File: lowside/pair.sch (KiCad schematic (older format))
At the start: 13 parts, among them U1 VNLD5090

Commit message: add 7th pair
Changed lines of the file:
@@
 $Descr A4 11693 8268
 encoding utf-8
-Sheet 2 7
+Sheet 8 8
 Title ""
 Date ""
@@
 AR Path="/5E2D1A09/5E28FEFB" Ref="U5"  Part="1"
 AR Path="/5E2D1A0F/5E28FEFB" Ref="U6"  Part="1"
-F 0 "U1" H 3100 2547 60  0000 C CNN
+AR Path="/5E2B6330/5E28FEFB" Ref="U7"  Part="1"
+F 0 "U7" H 3100 2547 60  0000 C CNN
 F 1 "VNLD5090" H 3100 2441 60  0000 C CNN
 F 2 "Package_SO:SO-8_3.9x4.9mm_P1.27mm" H 3200 1650 60  0001 C CNN
@@
 AR Path="/5E2D1A09/5E290D55" Ref="#PWR0153"  Part="1"
 AR Path="/5E2D1A0F/5E290D55" Ref="#PWR0163"  Part="1"
-F 0 "#PWR0113" H 3300 2250 50  0001 C CNN
+AR Path="/5E2B6330/5E290D55" Ref="#PWR0177"  Part="1"
+F 0 "#PWR0177" H 3300 2250 50  0001 C CNN
 F 1 "GND" H 3305 2327 50  0000 C CNN
 F 2 "" H 3300 2500 50  0001 C CNN
@@
 AR Path="/5E2D1A09/5E291066" Ref="#PWR0154"  Part="1"
 AR Path="/5E2D1A0F/5E291066" Ref="#PWR0164"  Part="1"
-F 0 "#PWR0114" H 3400 2250 50  0001 C CNN
+AR Path="/5E2B6330/5E291066" Ref="#PWR0178"  Part="1"
+F 0 "#PWR0178" H 3400 2250 50  0001 C CNN
 F 1 "GND" H 3405 2327 50  0000 C CNN
 F 2 "" H 3400 2500 50  0001 C CNN
@@
 AR Path="/5E2D1A09/5E291CC1" Ref="R25"  Part="1"
 AR Path="/5E2D1A0F/5E291CC1" Ref="R31"  Part="1"
-F 0 "R1" V 2100 1500 50  0000 C CNN
+AR Path="/5E2B6330/5E291CC1" Ref="R39"  Part="1"
+F 0 "R39" V 2100 1500 50  0000 C CNN
 F 1 "1k" V 2200 1500 50  0000 C CNN
 F 2 "Resistor_SMD:R_0603_1608Metric" V 2130 1500 50  0001 C CNN
@@
 AR Path="/5E2D1A09/5E292256" Ref="R26"  Part="1"
 AR Path="/5E2D1A0F/5E292256" Ref="R32"  Part="1"
-F 0 "R2" V 2300 2050 50  0000 C CNN
+AR Path="/5E2B6330/5E292256" Ref="R40"  Part="1"
+F 0 "R40" V 2300 2050 50  0000 C CNN
 F 1 "1k" V 2200 2050 50  0000 C CNN
 F 2 "Resistor_SMD:R_0603_1608Metric" V 2130 2050 50  0001 C CNN
@@
 AR Path="/5E2D1A09/5E2928C2" Ref="C9"  Part="1"
 AR Path="/5E2D1A0F/5E2928C2" Ref="C11"  Part="1"
-F 0 "C1" H 3635 1204 50  0000 R CNN
+AR Path="/5E2B6330/5E2928C2" Ref="C13"  Part="1"
+F 0 "C13" H 3635 1204 50  0000 R CNN
 F 1 "6.8n" H 3635 1295 50  0000 R CNN
 F 2 "Capacitor_SMD:C_0603_1608Metric" H 3788 1100 50  0001 C CNN
@@
 AR Path="/5E2D1A09/5E293060" Ref="C10"  Part="1"
 AR Path="/5E2D1A0F/5E293060" Ref="C12"  Part="1"
-F 0 "C2" H 3865 2346 50  0000 L CNN
+AR Path="/5E2B6330/5E293060" Ref="C14"  Part="1"
+F 0 "C14" H 3865 2346 50  0000 L CNN
 F 1 "6.8n" H 3865 2255 50  0000 L CNN
 F 2 "Capacitor_SMD:C_0603_1608Metric" H 3788 2150 50  0001 C CNN
@@
 AR Path="/5E2D1A09/5E293508" Ref="#PWR0155"  Part="1"
 AR Path="/5E2D1A0F/5E293508" Ref="#PWR0165"  Part="1"
-F 0 "#PWR0115" H 3750 850 50  0001 C CNN
+AR Path="/5E2B6330/5E293508" Ref="#PWR0179"  Part="1"
+F 0 "#PWR0179" H 3750 850 50  0001 C CNN
 F 1 "GND" H 3755 927 50  0000 C CNN
 F 2 "" H 3750 1100 50  0001 C CNN
@@
 AR Path="/5E2D1A09/5E294C43" Ref="#PWR0156"  Part="1"
 AR Path="/5E2D1A0F/5E294C43" Ref="#PWR0166"  Part="1"
-F 0 "#PWR0116" H 3750 2200 50  0001 C CNN
+AR Path="/5E2B6330/5E294C43" Ref="#PWR0180"  Part="1"
+F 0 "#PWR0180" H 3750 2200 50  0001 C CNN
 F 1 "GND" H 3755 2277 50  0000 C CNN
 F 2 "" H 3750 2450 50  0001 C CNN
@@
 AR Path="/5E2D1A09/5E295706" Ref="#PWR0157"  Part="1"
 AR Path="/5E2D1A0F/5E295706" Ref="#PWR0167"  Part="1"
-F 0 "#PWR0117" H 2450 2350 50  0001 C CNN
+AR Path="/5E2B6330/5E295706" Ref="#PWR0181"  Part="1"
+F 0 "#PWR0181" H 2450 2350 50  0001 C CNN
 F 1 "GND" H 2455 2427 50  0000 C CNN
 F 2 "" H 2450 2600 50  0001 C CNN
@@
 AR Path="/5E2D1A09/5E295C01" Ref="R28"  Part="1"
 AR Path="/5E2D1A0F/5E295C01" Ref="R34"  Part="1"
-F 0 "R4" V 2350 2400 50  0000 L CNN
+AR Path="/5E2B6330/5E295C01" Ref="R42"  Part="1"
+F 0 "R42" V 2350 2400 50  0000 L CNN
 F 1 "10k" V 2450 2350 50  0000 L CNN
 F 2 "Resistor_SMD:R_0603_1608Metric" V 2380 2450 50  0001 C CNN
@@
 AR Path="/5E2D1A09/5E295EF2" Ref="R27"  Part="1"
 AR Path="/5E2D1A0F/5E295EF2" Ref="R33"  Part="1"
-F 0 "R3" V 2550 1200 50  0000 L CNN
+AR Path="/5E2B6330/5E295EF2" Ref="R41"  Part="1"
+F 0 "R41" V 2550 1200 50  0000 L CNN
 F 1 "10k" V 2450 1200 50  0000 L CNN
 F 2 "Resistor_SMD:R_0603_1608Metric" V 2380 1250 50  0001 C CNN
@@
 AR Path="/5E2D1A09/5E297A73" Ref="#PWR0158"  Part="1"
 AR Path="/5E2D1A0F/5E297A73" Ref="#PWR0168"  Part="1"
-F 0 "#PWR0118" H 2450 850 50  0001 C CNN
+AR Path="/5E2B6330/5E297A73" Ref="#PWR0182"  Part="1"
+F 0 "#PWR0182" H 2450 850 50  0001 C CNN
 F 1 "GND" H 2455 927 50  0000 C CNN
 F 2 "" H 2450 1100 50  0001 C CNN
@@
 AR Path="/5E2D1A09/5E2A21C5" Ref="D17"  Part="1"
 AR Path="/5E2D1A0F/5E2A21C5" Ref="D21"  Part="1"
-F 0 "D1" V 4204 1329 50  0000 L CNN
+AR Path="/5E2B6330/5E2A21C5" Ref="D27"  Part="1"
+F 0 "D27" V 4204 1329 50  0000 L CNN
 F 1 "D_Schottky" V 4295 1329 50  0000 L CNN
 F 2 "Diode_SMD:D_SMF" H 4250 1250 50  0001 C CNN
@@
 AR Path="/5E2D1A09/5E2A29A5" Ref="#PWR0159"  Part="1"
 AR Path="/5E2D1A0F/5E2A29A5" Ref="#PWR0169"  Part="1"
-F 0 "#PWR0137" H 4250 950 50  0001 C CNN
+AR Path="/5E2B6330/5E2A29A5" Ref="#PWR0183"  Part="1"
+F 0 "#PWR0183" H 4250 950 50  0001 C CNN
 F 1 "+12V" H 4265 1273 50  0000 C CNN
 F 2 "" H 4250 1100 50  0001 C CNN
@@
 AR Path="/5E2D1A09/5E2A30AB" Ref="D18"  Part="1"
 AR Path="/5E2D1A0F/5E2A30AB" Ref="D22"  Part="1"
-F 0 "D2" V 4296 2221 50  0000 R CNN
+AR Path="/5E2B6330/5E2A30AB" Ref="D28"  Part="1"
+F 0 "D28" V 4296 2221 50  0000 R CNN
 F 1 "D_Schottky" V 4205 2221 50  0000 R CNN
 F 2 "Diode_SMD:D_SMF" H 4250 2300 50  0001 C CNN
@@
 AR Path="/5E2D1A09/5E2A3E5A" Ref="#PWR0160"  Part="1"
 AR Path="/5E2D1A0F/5E2A3E5A" Ref="#PWR0170"  Part="1"
-F 0 "#PWR0138" H 4250 2300 50  0001 C CNN
+AR Path="/5E2B6330/5E2A3E5A" Ref="#PWR0184"  Part="1"
+F 0 "#PWR0184" H 4250 2300 50  0001 C CNN
 F 1 "+12V" H 4265 2623 50  0000 C CNN
 F 2 "" H 4250 2450 50  0001 C CNN
@@
 AR Path="/5E2D1A09/5E2BF0E5" Ref="D20"  Part="1"
 AR Path="/5E2D1A0F/5E2BF0E5" Ref="D24"  Part="1"
-F 0 "D10" V 4897 2378 50  0000 L CNN
+AR Path="/5E2B6330/5E2BF0E5" Ref="D30"  Part="1"
+F 0 "D30" V 4897 2378 50  0000 L CNN
 F 1 "LED" V 4988 2378 50  0000 L CNN
 F 2 "LED_SMD:LED_0603_1608Metric" H 4950 2300 50  0001 C CNN
@@
 AR Path="/5E2D1A09/5E2C027A" Ref="#PWR0161"  Part="1"
 AR Path="/5E2D1A0F/5E2C027A" Ref="#PWR0171"  Part="1"
-F 0 "#PWR0145" H 4950 2600 50  0001 C CNN
+AR Path="/5E2B6330/5E2C027A" Ref="#PWR0185"  Part="1"
+F 0 "#PWR0185" H 4950 2600 50  0001 C CNN
 F 1 "+12V" H 4965 2923 50  0000 C CNN
 F 2 "" H 4950 2750 50  0001 C CNN
@@
 AR Path="/5E2D1A09/5E2C0BF3" Ref="R30"  Part="1"
 AR Path="/5E2D1A0F/5E2C0BF3" Ref="R36"  Part="1"
-F 0 "R18" H 5020 2646 50  0000 L CNN
+AR Path="/5E2B6330/5E2C0BF3" Ref="R44"  Part="1"
+F 0 "R44" H 5020 2646 50  0000 L CNN
 F 1 "1k" H 5020 2555 50  0000 L CNN
 F 2 "Resistor_SMD:R_0603_1608Metric" V 4880 2600 50  0001 C CNN
@@
 AR Path="/5E2D1A09/5E2C1564" Ref="D19"  Part="1"
 AR Path="/5E2D1A0F/5E2C1564" Ref="D23"  Part="1"
-F 0 "D9" V 4989 1133 50  0000 R CNN
+AR Path="/5E2B6330/5E2C1564" Ref="D29"  Part="1"
+F 0 "D29" V 4989 1133 50  0000 R CNN
 F 1 "LED" V 4898 1133 50  0000 R CNN
 F 2 "LED_SMD:LED_0603_1608Metric" H 4950 1250 50  0001 C CNN
@@
 AR Path="/5E2D1A09/5E2C1FBA" Ref="R29"  Part="1"
 AR Path="/5E2D1A0F/5E2C1FBA" Ref="R35"  Part="1"
-F 0 "R17" H 4880 904 50  0000 R CNN
+AR Path="/5E2B6330/5E2C1FBA" Ref="R43"  Part="1"
+F 0 "R43" H 4880 904 50  0000 R CNN
 F 1 "1k" H 4880 995 50  0000 R CNN
 F 2 "Resistor_SMD:R_0603_1608Metric" V 4880 950 50  0001 C CNN
@@
 AR Path="/5E2D1A09/5E2C2529" Ref="#PWR0162"  Part="1"
 AR Path="/5E2D1A0F/5E2C2529" Ref="#PWR0172"  Part="1"
-F 0 "#PWR0146" H 4950 650 50  0001 C CNN
+AR Path="/5E2B6330/5E2C2529" Ref="#PWR0186"  Part="1"
+F 0 "#PWR0186" H 4950 650 50  0001 C CNN
 F 1 "+12V" H 4965 973 50  0000 C CNN
 F 2 "" H 4950 800 50  0001 C CNN

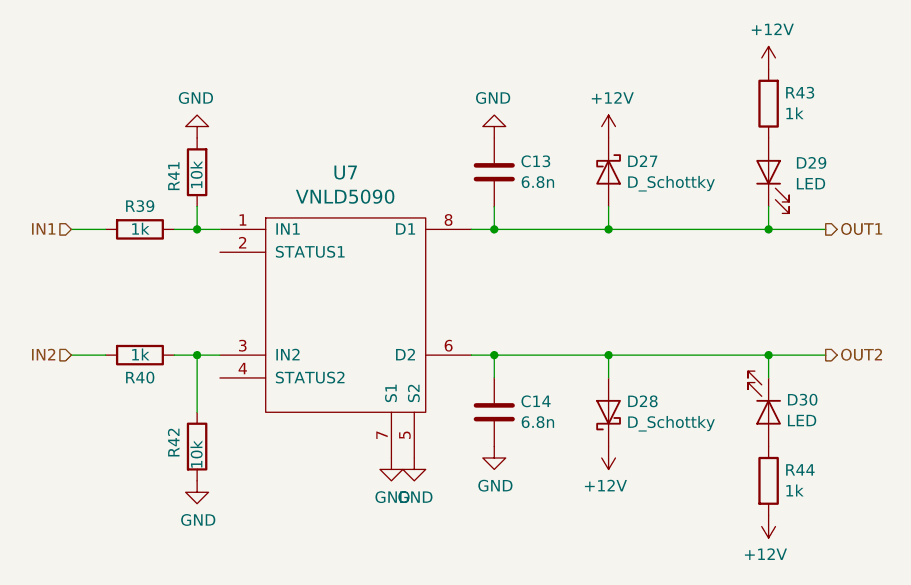
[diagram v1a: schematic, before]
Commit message: Updated properties in schematic closer to allowing BOM export.
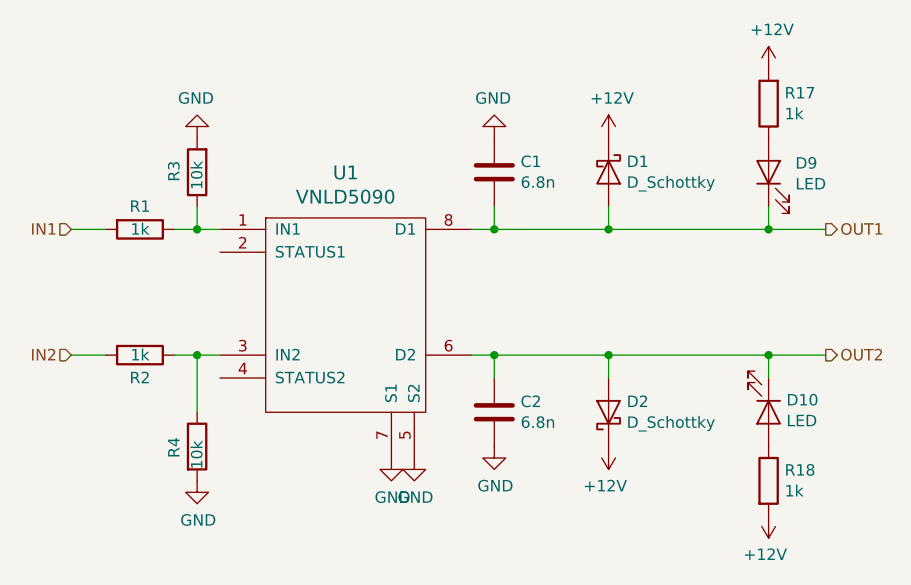
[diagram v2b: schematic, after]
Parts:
- C1, C2: MFG,MFG# (none) -> KE MET,C0603C682K1RACTU; Vend1,Vend1# (none) -> DIGI,399-3187-1-ND
- D1, D2: MFG,MFG# (none) -> LITTELFUSE,TPSMF4L36A; Vend1,Vend1# (none) -> DIGI,F7526CT-ND
- D15, D16: MFG,MFG# (none) -> DIALIGHT,598-8010-107F; Vend1,Vend1# (none) -> DIGI,350-2029-1-ND
- R1, R2, R23, R24: MFG,MFG# (none) -> YAGEO,RC0603JR-071KL; Vend1,Vend1# (none) -> DIGI,311-1.0KGRCT-ND
- R3, R4: MFG,MFG# (none) -> YAGEO,RC0603JR-0710KL; Vend1,Vend1# (none) -> DIGI,311-10KGRCT-ND
- U1: MFG,MFG# (none) -> ST,VNLD5090TR-E; Vend1,Vend1# (none) -> DIGI,497-14323-1-ND
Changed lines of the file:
@@
 $Descr A4 11693 8268
 encoding utf-8
-Sheet 8 8
+Sheet 2 8
 Title ""
 Date ""
@@
 AR Path="/5E2D1A0F/5E28FEFB" Ref="U6"  Part="1"
 AR Path="/5E2B6330/5E28FEFB" Ref="U7"  Part="1"
-F 0 "U7" H 3100 2547 60  0000 C CNN
+F 0 "U1" H 3100 2547 60  0000 C CNN
 F 1 "VNLD5090" H 3100 2441 60  0000 C CNN
 F 2 "Package_SO:SO-8_3.9x4.9mm_P1.27mm" H 3200 1650 60  0001 C CNN
 F 3 "" H 3200 1650 60  0001 C CNN
+F 4 "ST,VNLD5090TR-E" H 3100 1900 50  0001 C CNN "MFG,MFG#"
+F 5 "DIGI,497-14323-1-ND" H 3100 1900 50  0001 C CNN "Vend1,Vend1#"
 	1    3100 1900
 	1    0    0    -1
@@
 AR Path="/5E2D1A0F/5E290D55" Ref="#PWR0163"  Part="1"
 AR Path="/5E2B6330/5E290D55" Ref="#PWR0177"  Part="1"
-F 0 "#PWR0177" H 3300 2250 50  0001 C CNN
+F 0 "#PWR0113" H 3300 2250 50  0001 C CNN
 F 1 "GND" H 3305 2327 50  0000 C CNN
 F 2 "" H 3300 2500 50  0001 C CNN
@@
 AR Path="/5E2D1A0F/5E291066" Ref="#PWR0164"  Part="1"
 AR Path="/5E2B6330/5E291066" Ref="#PWR0178"  Part="1"
-F 0 "#PWR0178" H 3400 2250 50  0001 C CNN
+F 0 "#PWR0114" H 3400 2250 50  0001 C CNN
 F 1 "GND" H 3405 2327 50  0000 C CNN
 F 2 "" H 3400 2500 50  0001 C CNN
@@
 AR Path="/5E2D1A0F/5E291CC1" Ref="R31"  Part="1"
 AR Path="/5E2B6330/5E291CC1" Ref="R39"  Part="1"
-F 0 "R39" V 2100 1500 50  0000 C CNN
+F 0 "R1" V 2100 1500 50  0000 C CNN
 F 1 "1k" V 2200 1500 50  0000 C CNN
 F 2 "Resistor_SMD:R_0603_1608Metric" V 2130 1500 50  0001 C CNN
 F 3 "~" H 2200 1500 50  0001 C CNN
+F 4 "YAGEO,RC0603JR-071KL" H 2200 1500 50  0001 C CNN "MFG,MFG#"
+F 5 "DIGI,311-1.0KGRCT-ND" H 2200 1500 50  0001 C CNN "Vend1,Vend1#"
 	1    2200 1500
 	0    1    1    0
@@
 AR Path="/5E2D1A0F/5E292256" Ref="R32"  Part="1"
 AR Path="/5E2B6330/5E292256" Ref="R40"  Part="1"
-F 0 "R40" V 2300 2050 50  0000 C CNN
+F 0 "R2" V 2300 2050 50  0000 C CNN
 F 1 "1k" V 2200 2050 50  0000 C CNN
 F 2 "Resistor_SMD:R_0603_1608Metric" V 2130 2050 50  0001 C CNN
 F 3 "~" H 2200 2050 50  0001 C CNN
+F 4 "YAGEO,RC0603JR-071KL" H 2200 2050 50  0001 C CNN "MFG,MFG#"
+F 5 "DIGI,311-1.0KGRCT-ND" H 2200 2050 50  0001 C CNN "Vend1,Vend1#"
 	1    2200 2050
 	0    1    1    0
@@
 AR Path="/5E2D1A0F/5E2928C2" Ref="C11"  Part="1"
 AR Path="/5E2B6330/5E2928C2" Ref="C13"  Part="1"
-F 0 "C13" H 3635 1204 50  0000 R CNN
+F 0 "C1" H 3635 1204 50  0000 R CNN
 F 1 "6.8n" H 3635 1295 50  0000 R CNN
 F 2 "Capacitor_SMD:C_0603_1608Metric" H 3788 1100 50  0001 C CNN
 F 3 "~" H 3750 1250 50  0001 C CNN
+F 4 "KE MET,C0603C682K1RACTU" H 3750 1250 50  0001 C CNN "MFG,MFG#"
+F 5 "DIGI,399-3187-1-ND" H 3750 1250 50  0001 C CNN "Vend1,Vend1#"
 	1    3750 1250
 	-1   0    0    1
@@
 AR Path="/5E2D1A0F/5E293060" Ref="C12"  Part="1"
 AR Path="/5E2B6330/5E293060" Ref="C14"  Part="1"
-F 0 "C14" H 3865 2346 50  0000 L CNN
+F 0 "C2" H 3865 2346 50  0000 L CNN
 F 1 "6.8n" H 3865 2255 50  0000 L CNN
 F 2 "Capacitor_SMD:C_0603_1608Metric" H 3788 2150 50  0001 C CNN
 F 3 "~" H 3750 2300 50  0001 C CNN
+F 4 "KE MET,C0603C682K1RACTU" H 3750 2300 50  0001 C CNN "MFG,MFG#"
+F 5 "DIGI,399-3187-1-ND" H 3750 2300 50  0001 C CNN "Vend1,Vend1#"
 	1    3750 2300
 	1    0    0    -1
@@
 AR Path="/5E2D1A0F/5E293508" Ref="#PWR0165"  Part="1"
 AR Path="/5E2B6330/5E293508" Ref="#PWR0179"  Part="1"
-F 0 "#PWR0179" H 3750 850 50  0001 C CNN
+F 0 "#PWR0115" H 3750 850 50  0001 C CNN
 F 1 "GND" H 3755 927 50  0000 C CNN
 F 2 "" H 3750 1100 50  0001 C CNN
@@
 AR Path="/5E2D1A0F/5E294C43" Ref="#PWR0166"  Part="1"
 AR Path="/5E2B6330/5E294C43" Ref="#PWR0180"  Part="1"
-F 0 "#PWR0180" H 3750 2200 50  0001 C CNN
+F 0 "#PWR0116" H 3750 2200 50  0001 C CNN
 F 1 "GND" H 3755 2277 50  0000 C CNN
 F 2 "" H 3750 2450 50  0001 C CNN
@@
 AR Path="/5E2D1A0F/5E295706" Ref="#PWR0167"  Part="1"
 AR Path="/5E2B6330/5E295706" Ref="#PWR0181"  Part="1"
-F 0 "#PWR0181" H 2450 2350 50  0001 C CNN
+F 0 "#PWR0117" H 2450 2350 50  0001 C CNN
 F 1 "GND" H 2455 2427 50  0000 C CNN
 F 2 "" H 2450 2600 50  0001 C CNN
@@
 AR Path="/5E2D1A0F/5E295C01" Ref="R34"  Part="1"
 AR Path="/5E2B6330/5E295C01" Ref="R42"  Part="1"
-F 0 "R42" V 2350 2400 50  0000 L CNN
+F 0 "R4" V 2350 2400 50  0000 L CNN
 F 1 "10k" V 2450 2350 50  0000 L CNN
 F 2 "Resistor_SMD:R_0603_1608Metric" V 2380 2450 50  0001 C CNN
 F 3 "~" H 2450 2450 50  0001 C CNN
+F 4 "YAGEO,RC0603JR-0710KL" H 2450 2450 50  0001 C CNN "MFG,MFG#"
+F 5 "DIGI,311-10KGRCT-ND" H 2450 2450 50  0001 C CNN "Vend1,Vend1#"
 	1    2450 2450
 	1    0    0    -1
@@
 AR Path="/5E2D1A0F/5E295EF2" Ref="R33"  Part="1"
 AR Path="/5E2B6330/5E295EF2" Ref="R41"  Part="1"
-F 0 "R41" V 2550 1200 50  0000 L CNN
+F 0 "R3" V 2550 1200 50  0000 L CNN
 F 1 "10k" V 2450 1200 50  0000 L CNN
 F 2 "Resistor_SMD:R_0603_1608Metric" V 2380 1250 50  0001 C CNN
 F 3 "~" H 2450 1250 50  0001 C CNN
+F 4 "YAGEO,RC0603JR-0710KL" H 2450 1250 50  0001 C CNN "MFG,MFG#"
+F 5 "DIGI,311-10KGRCT-ND" H 2450 1250 50  0001 C CNN "Vend1,Vend1#"
 	1    2450 1250
 	-1   0    0    1
@@
 AR Path="/5E2D1A0F/5E297A73" Ref="#PWR0168"  Part="1"
 AR Path="/5E2B6330/5E297A73" Ref="#PWR0182"  Part="1"
-F 0 "#PWR0182" H 2450 850 50  0001 C CNN
+F 0 "#PWR0118" H 2450 850 50  0001 C CNN
 F 1 "GND" H 2455 927 50  0000 C CNN
 F 2 "" H 2450 1100 50  0001 C CNN
@@
 AR Path="/5E2D1A0F/5E2A21C5" Ref="D21"  Part="1"
 AR Path="/5E2B6330/5E2A21C5" Ref="D27"  Part="1"
-F 0 "D27" V 4204 1329 50  0000 L CNN
+F 0 "D1" V 4204 1329 50  0000 L CNN
 F 1 "D_Schottky" V 4295 1329 50  0000 L CNN
 F 2 "Diode_SMD:D_SMF" H 4250 1250 50  0001 C CNN
 F 3 "~" H 4250 1250 50  0001 C CNN
+F 4 "LITTELFUSE,TPSMF4L36A" H 4250 1250 50  0001 C CNN "MFG,MFG#"
+F 5 "DIGI,F7526CT-ND" H 4250 1250 50  0001 C CNN "Vend1,Vend1#"
 	1    4250 1250
 	0    1    1    0
@@
 AR Path="/5E2D1A0F/5E2A29A5" Ref="#PWR0169"  Part="1"
 AR Path="/5E2B6330/5E2A29A5" Ref="#PWR0183"  Part="1"
-F 0 "#PWR0183" H 4250 950 50  0001 C CNN
+F 0 "#PWR0137" H 4250 950 50  0001 C CNN
 F 1 "+12V" H 4265 1273 50  0000 C CNN
 F 2 "" H 4250 1100 50  0001 C CNN
@@
 AR Path="/5E2D1A0F/5E2A30AB" Ref="D22"  Part="1"
 AR Path="/5E2B6330/5E2A30AB" Ref="D28"  Part="1"
-F 0 "D28" V 4296 2221 50  0000 R CNN
+F 0 "D2" V 4296 2221 50  0000 R CNN
 F 1 "D_Schottky" V 4205 2221 50  0000 R CNN
 F 2 "Diode_SMD:D_SMF" H 4250 2300 50  0001 C CNN
 F 3 "~" H 4250 2300 50  0001 C CNN
+F 4 "LITTELFUSE,TPSMF4L36A" H 4250 2300 50  0001 C CNN "MFG,MFG#"
+F 5 "DIGI,F7526CT-ND" H 4250 2300 50  0001 C CNN "Vend1,Vend1#"
 	1    4250 2300
 	0    -1   -1   0
@@
 AR Path="/5E2D1A0F/5E2A3E5A" Ref="#PWR0170"  Part="1"
 AR Path="/5E2B6330/5E2A3E5A" Ref="#PWR0184"  Part="1"
-F 0 "#PWR0184" H 4250 2300 50  0001 C CNN
+F 0 "#PWR0138" H 4250 2300 50  0001 C CNN
 F 1 "+12V" H 4265 2623 50  0000 C CNN
 F 2 "" H 4250 2450 50  0001 C CNN
@@
 AR Path="/5E2D1A0F/5E2BF0E5" Ref="D24"  Part="1"
 AR Path="/5E2B6330/5E2BF0E5" Ref="D30"  Part="1"
-F 0 "D30" V 4897 2378 50  0000 L CNN
+F 0 "D10" V 4897 2378 50  0000 L CNN
 F 1 "LED" V 4988 2378 50  0000 L CNN
 F 2 "LED_SMD:LED_0603_1608Metric" H 4950 2300 50  0001 C CNN
 F 3 "~" H 4950 2300 50  0001 C CNN
+F 4 "DIALIGHT,598-8010-107F" H 4950 2300 50  0001 C CNN "MFG,MFG#"
+F 5 "DIGI,350-2029-1-ND" H 4950 2300 50  0001 C CNN "Vend1,Vend1#"
 	1    4950 2300
 	0    1    1    0
@@
 AR Path="/5E2D1A0F/5E2C027A" Ref="#PWR0171"  Part="1"
 AR Path="/5E2B6330/5E2C027A" Ref="#PWR0185"  Part="1"
-F 0 "#PWR0185" H 4950 2600 50  0001 C CNN
+F 0 "#PWR0145" H 4950 2600 50  0001 C CNN
 F 1 "+12V" H 4965 2923 50  0000 C CNN
 F 2 "" H 4950 2750 50  0001 C CNN
@@
 AR Path="/5E2D1A0F/5E2C0BF3" Ref="R36"  Part="1"
 AR Path="/5E2B6330/5E2C0BF3" Ref="R44"  Part="1"
-F 0 "R44" H 5020 2646 50  0000 L CNN
+F 0 "R18" H 5020 2646 50  0000 L CNN
 F 1 "1k" H 5020 2555 50  0000 L CNN
 F 2 "Resistor_SMD:R_0603_1608Metric" V 4880 2600 50  0001 C CNN
 F 3 "~" H 4950 2600 50  0001 C CNN
+F 4 "YAGEO,RC0603JR-071KL" H 4950 2600 50  0001 C CNN "MFG,MFG#"
+F 5 "DIGI,311-1.0KGRCT-ND" H 4950 2600 50  0001 C CNN "Vend1,Vend1#"
 	1    4950 2600
 	1    0    0    -1
@@
 AR Path="/5E2D1A0F/5E2C1564" Ref="D23"  Part="1"
 AR Path="/5E2B6330/5E2C1564" Ref="D29"  Part="1"
-F 0 "D29" V 4989 1133 50  0000 R CNN
+F 0 "D9" V 4989 1133 50  0000 R CNN
 F 1 "LED" V 4898 1133 50  0000 R CNN
 F 2 "LED_SMD:LED_0603_1608Metric" H 4950 1250 50  0001 C CNN
 F 3 "~" H 4950 1250 50  0001 C CNN
+F 4 "DIALIGHT,598-8010-107F" H 4950 1250 50  0001 C CNN "MFG,MFG#"
+F 5 "DIGI,350-2029-1-ND" H 4950 1250 50  0001 C CNN "Vend1,Vend1#"
 	1    4950 1250
 	0    -1   -1   0
@@
 AR Path="/5E2D1A0F/5E2C1FBA" Ref="R35"  Part="1"
 AR Path="/5E2B6330/5E2C1FBA" Ref="R43"  Part="1"
-F 0 "R43" H 4880 904 50  0000 R CNN
+F 0 "R17" H 4880 904 50  0000 R CNN
 F 1 "1k" H 4880 995 50  0000 R CNN
 F 2 "Resistor_SMD:R_0603_1608Metric" V 4880 950 50  0001 C CNN
 F 3 "~" H 4950 950 50  0001 C CNN
+F 4 "YAGEO,RC0603JR-071KL" H 4950 950 50  0001 C CNN "MFG,MFG#"
+F 5 "DIGI,311-1.0KGRCT-ND" H 4950 950 50  0001 C CNN "Vend1,Vend1#"
 	1    4950 950
 	-1   0    0    1
@@
 AR Path="/5E2D1A0F/5E2C2529" Ref="#PWR0172"  Part="1"
 AR Path="/5E2B6330/5E2C2529" Ref="#PWR0186"  Part="1"
-F 0 "#PWR0186" H 4950 650 50  0001 C CNN
+F 0 "#PWR0146" H 4950 650 50  0001 C CNN
 F 1 "+12V" H 4965 973 50  0000 C CNN
 F 2 "" H 4950 800 50  0001 C CNN

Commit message: Generated gerbers and BOM for MFG.
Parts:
- D1, D2: MFG,MFG# LITTELFUSE,TPSMF4L36A -> DIODES_INC,SBR2U60S1F; Vend1,Vend1# DIGI,F7526CT-ND -> DIGI,SBR2U60S1F-7DICT-ND
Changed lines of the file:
@@
 F 2 "Diode_SMD:D_SMF" H 4250 1250 50  0001 C CNN
 F 3 "~" H 4250 1250 50  0001 C CNN
-F 4 "LITTELFUSE,TPSMF4L36A" H 4250 1250 50  0001 C CNN "MFG,MFG#"
-F 5 "DIGI,F7526CT-ND" H 4250 1250 50  0001 C CNN "Vend1,Vend1#"
+F 4 "DIODES_INC,SBR2U60S1F" H 4250 1250 50  0001 C CNN "MFG,MFG#"
+F 5 "DIGI,SBR2U60S1F-7DICT-ND" H 4250 1250 50  0001 C CNN "Vend1,Vend1#"
 	1    4250 1250
 	0    1    1    0
@@
 F 2 "Diode_SMD:D_SMF" H 4250 2300 50  0001 C CNN
 F 3 "~" H 4250 2300 50  0001 C CNN
-F 4 "LITTELFUSE,TPSMF4L36A" H 4250 2300 50  0001 C CNN "MFG,MFG#"
-F 5 "DIGI,F7526CT-ND" H 4250 2300 50  0001 C CNN "Vend1,Vend1#"
+F 4 "DIODES_INC,SBR2U60S1F" H 4250 2300 50  0001 C CNN "MFG,MFG#"
+F 5 "DIGI,SBR2U60S1F-7DICT-ND" H 4250 2300 50  0001 C CNN "Vend1,Vend1#"
 	1    4250 2300
 	0    -1   -1   0
